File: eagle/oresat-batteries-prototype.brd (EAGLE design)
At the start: 42 x 63 mm, 85 parts, among them Q1 PMV45EN, Q10 NTR4101P, Q11 NTR4101P, Q12 Si7625DN, Q13 Si7625DN, Q14 Si7625DN, Q15 Si7625DN, Q16 Si7625DN, Q2 Si7625DN, Q3 PMV45EN, Q4 PMV45EN, Q5 PMV45EN, Q6 PMV45EN, Q7 PMV45EN, Q9 Si7625DN, U10 LTC4412, U11 S-8209AAA-T8T1U, U12 S-8209AAA-T8T1U, U2 MAX17205G, U9 LTC4412

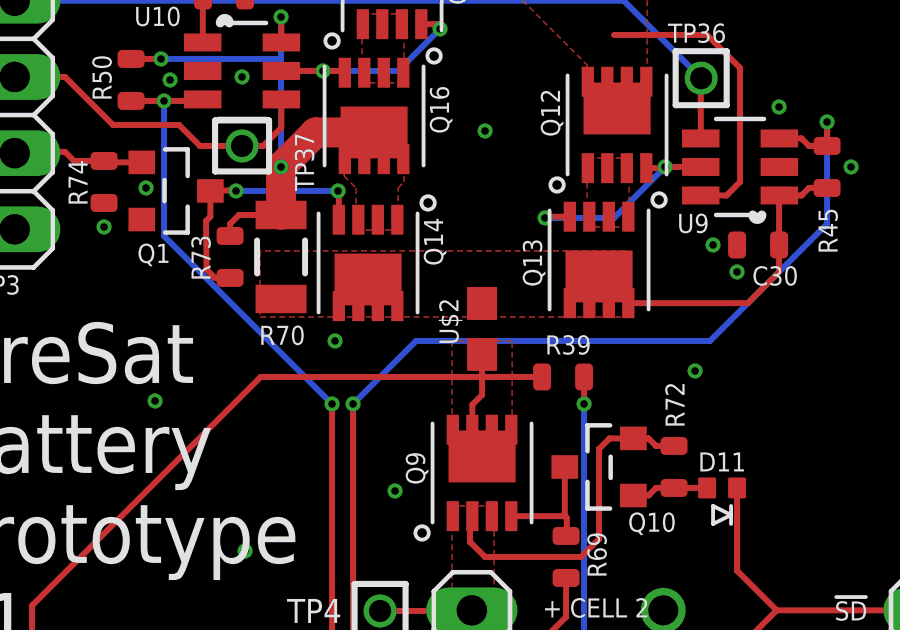
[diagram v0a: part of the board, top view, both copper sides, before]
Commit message: Finalized battery prototype, choose parts, made BOM, ordered!
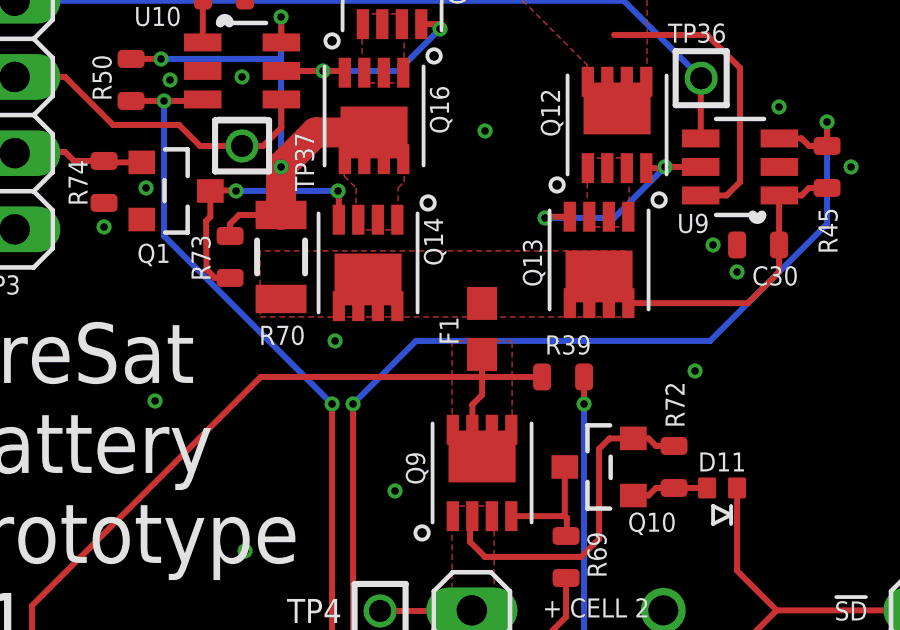
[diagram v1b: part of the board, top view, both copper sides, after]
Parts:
- renumbered U$2 to F1
